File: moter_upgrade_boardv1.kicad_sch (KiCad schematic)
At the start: 51 parts, among them J1 Conn_01x04_Socket, J2 Conn_01x03_Socket, J3 Conn_01x03_Socket, J4 Conn_01x02_Socket, J5 Conn_01x05_Socket, J6 USB_C_Receptacle_USB2.0_16P, J7 Conn_01x02_Socket, SW1 SW_SPDT, SW2 SW_Push, SW3 SW_Wuerth_450301014042, U1 BD33FC0FP, U2 TLP785, U3 TLP785, U4 STM32H523CCTx, U5 MCP2562-E-P, U6 CH340E, U7 BD33FC0FP

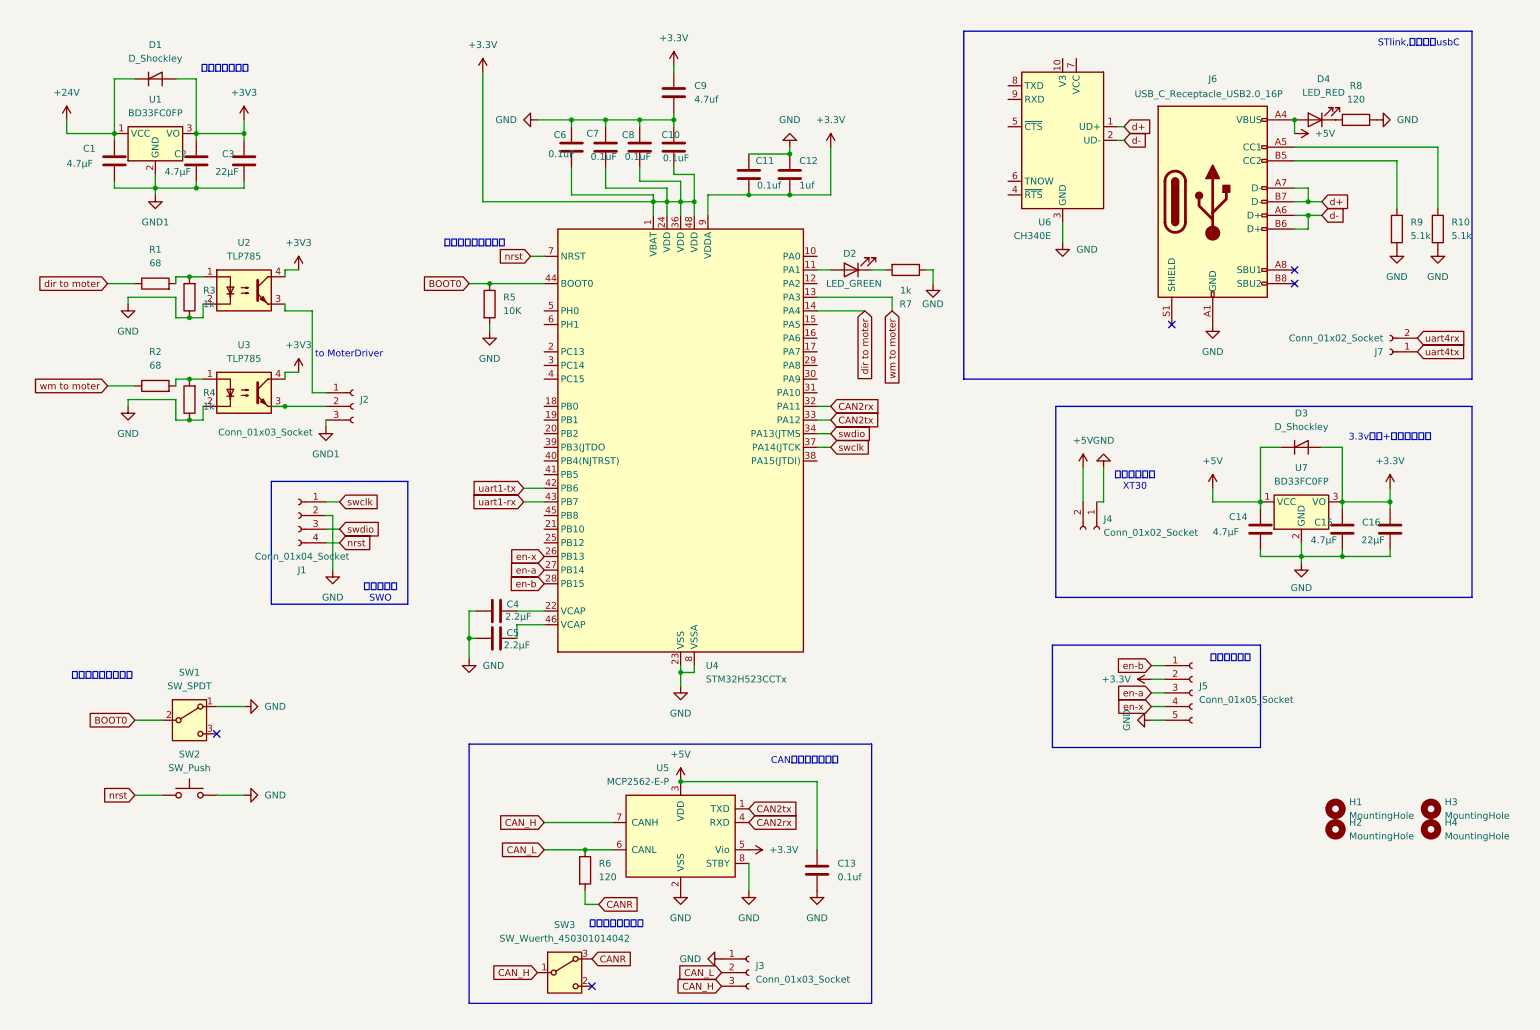
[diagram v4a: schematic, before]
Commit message: フットプリントの一部変更と部品配置
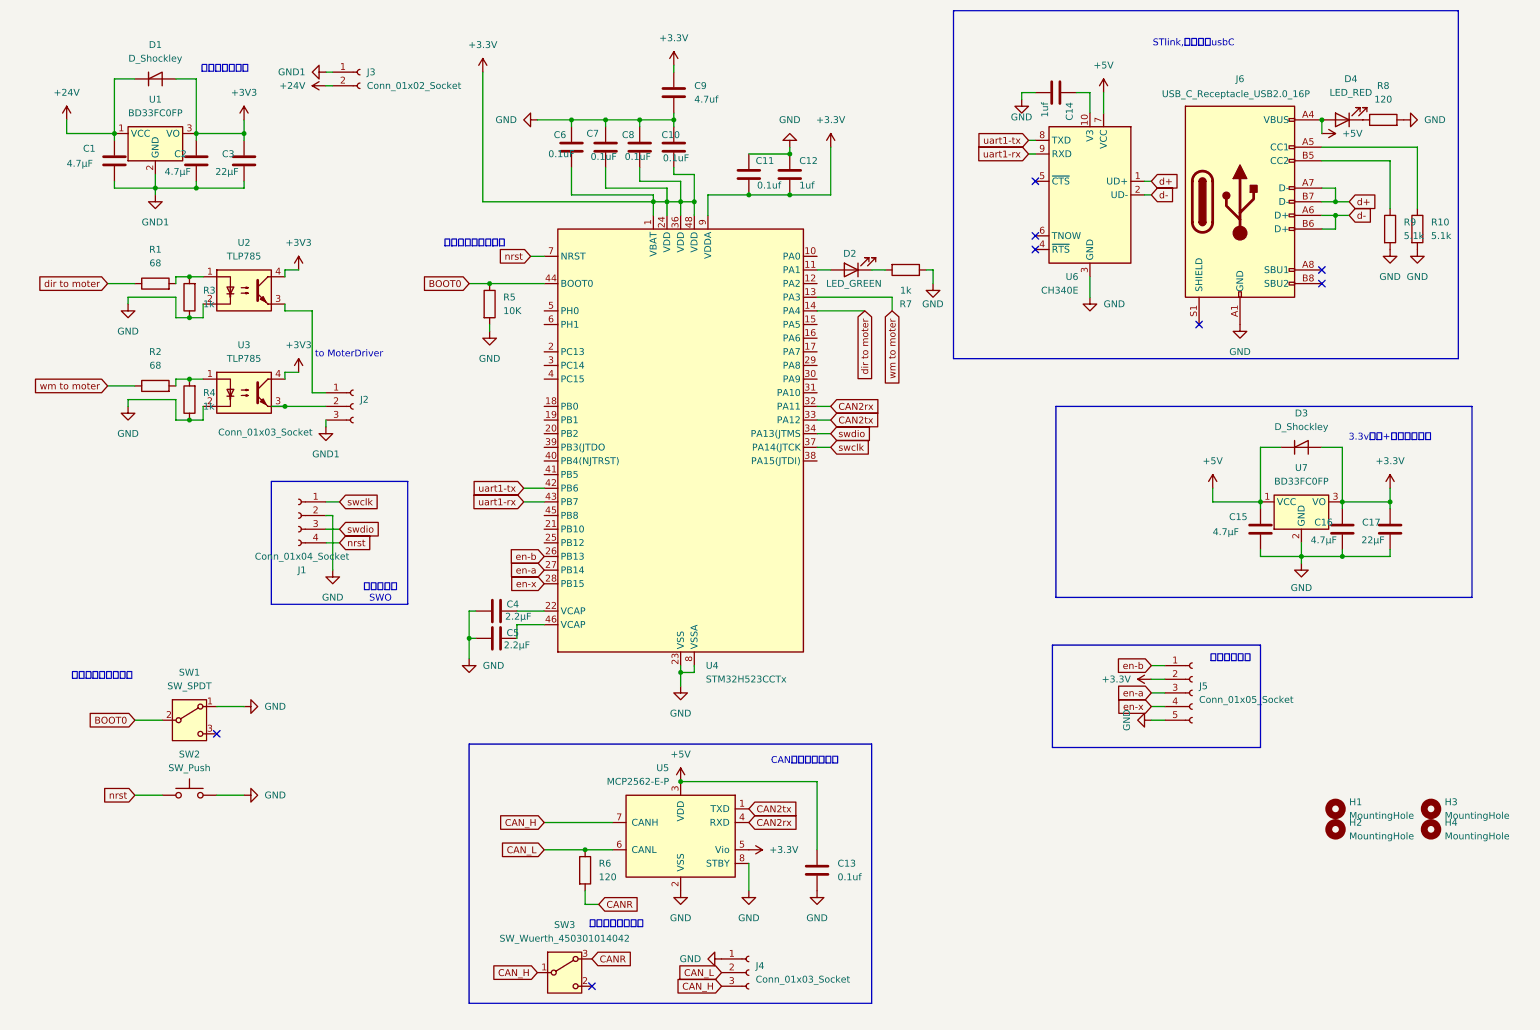
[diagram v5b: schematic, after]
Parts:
- removed J4: Conn_01x02_Socket, Connector_AMASS:AMASS_XT30PW-F_1x02_P2.50mm_Horizontal, symbol Connector:Conn_01x02_Socket
- removed J7: Conn_01x02_Socket, Connector_JST:JST_XH_S2B-XH-A-1_1x02_P2.50mm_Horizontal, symbol Connector:Conn_01x02_Socket
- added C14: 1uf, Capacitor_SMD:C_0603_1608Metric_Pad1.08x0.95mm_HandSolder, symbol Device:C
- added J3: Conn_01x02_Socket, Connector_AMASS:AMASS_XT30PW-M_1x02_P2.50mm_Horizontal, symbol Connector:Conn_01x02_Socket
- J1: footprint Connector_JST:JST_XH_S4B-XH-A-1_1x04_P2.50mm_Horizontal -> Connector_PinHeader_2.54mm:PinHeader_1x04_P2.54mm_Vertical
- R1, R2: footprint Resistor_THT:R_Axial_DIN0207_L6.3mm_D2.5mm_P10.16mm_Horizontal -> Resistor_SMD:R_0603_1608Metric_Pad0.98x0.95mm_HandSolder
- renumbered C14 to C15, C15 to C16, C16 to C17, J3 to J4
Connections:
- net +24V: now also J3.2 (Pin_2)
- net +5V: now also U6.7 (VCC)
- net GND: now also C14.2
- net GND1: now also J3.1 (Pin_1)
- net en-b: now also U4.26 (PB13); no longer U4.28 (PB15)
- net en-x: now also U4.28 (PB15); no longer U4.26 (PB13)
- net uart1-rx: now also U6.9 (RXD)
- net uart1-tx: now also U6.8 (TXD)
- net at U6.10 (V3): now also C14.1
- no-connect marks 5 -> 8
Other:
- note removed: "電源コネクタ XT30"
- moved on the sheet: D4, J6, R10, R8, R9, U6

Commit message: 配線、配置変更など　いったん完成
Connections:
- net GND: now also J6.S1 (SHIELD)
- net dir to moter: now also U4.30 (PA9); no longer U4.14 (PA4)
- net wm to moter: now also U4.29 (PA8); no longer U4.13 (PA3)
- no-connect marks 8 -> 7

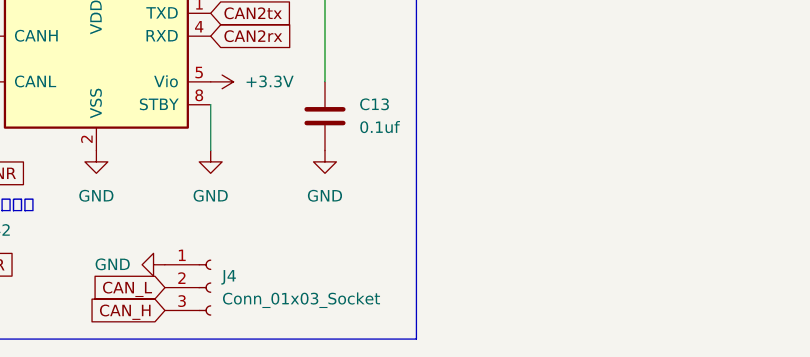
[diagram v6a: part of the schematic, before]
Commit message: CAN端子の追加
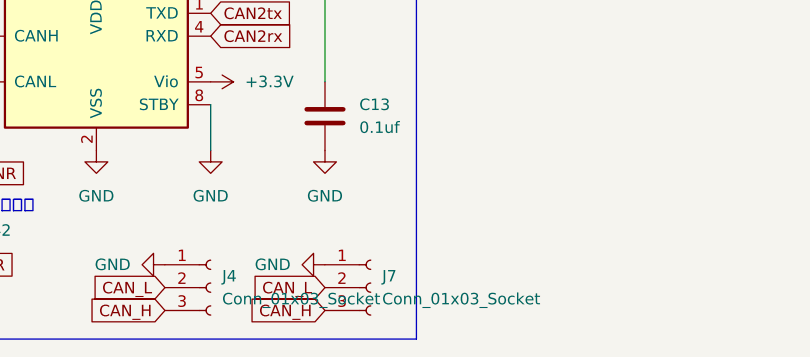
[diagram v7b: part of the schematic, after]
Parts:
- added J7: Conn_01x03_Socket, Connector_JST:JST_XH_B3B-XH-A_1x03_P2.50mm_Vertical, symbol Connector:Conn_01x03_Socket
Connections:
- net CAN_H: now also J7.3 (Pin_3)
- net CAN_L: now also J7.2 (Pin_2)
- net GND: now also J7.1 (Pin_1)

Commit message: usbCをもとに戻した　最終？？版
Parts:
- R8: value 120 -> 1k
